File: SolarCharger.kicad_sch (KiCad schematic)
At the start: 45 parts, among them U13 ADM1176-1ARMZ-R7

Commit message: v3.1 Updates
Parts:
- removed R110, R112: 0R, Resistor_SMD:R_0603_1608Metric, symbol Device:R_Small
- C4: renamed from C47; value 3.3nF -> 3n3
- R19: renamed from R25; value 100K -> 100k
- R21: renamed from R35; value 200K -> 200k
- R26: value 100K -> 100k
- R28: renamed from R89; value 200K -> 200k
- R33: renamed from R27; value 100K -> 100k
- R35: renamed from R109; value 200K -> 200k
- R36: renamed from R111; now not fitted
- R37: renamed from R113; now not fitted
- R38: renamed from R124; value ?R -> 0.01R
- R39: renamed from R125; value 1K -> 1k
- renumbered F6 to F2, F7 to F3, F8 to F4, F9 to F5, F10 to F6, R16 to R15, R17 to R16, R13 to R17, R22 to R18, R34 to R20, R18 to R22, R19 to R23, R14 to R24, R23 to R25, R88 to R27, R20 to R29, R21 to R30, R15 to R31, R24 to R32, R108 to R34, U13 to U2
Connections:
- net A0_S renamed A0
- net A1_S renamed A1
- net MPPT1/VIN renamed DSOLAR1
- net MPPT2/VIN renamed DSOLAR2
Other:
- sheet I2C Single Protection4 renamed I2C Single Protection2
- sheet I2C Single Protection5 renamed I2C Single Protection3
- note added: "#TODO: Check Resistor Values"
- note added: "I2C ADDR R36, R37 0R, 0R: 0x40 150k, 0R: 0x41 DNP, DNP: 0x4A 0R, DNP: 0x48"
- note removed: "I2C ADDR 0x4A Install R95: 0x48"
- company: (none) -> Carnegie Mellon University
- title: (none) -> Argus XY Solar Panel
- moved on the sheet: D1, D2, D3, D4, D5, F2, F3, F4, F5, R17, R18, R19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

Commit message: Local Stash
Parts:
- SC1, SC2, SC4, SC5, SC6: value SM141K06TF -> SM141K06TF/S; footprint Argus-Miscellaneous:SM141K06TF -> Argus-Miscellaneous:SM141K06TF_S
- SC3: value SM141K10TF -> SM141K10TF/S; footprint Argus-Miscellaneous:SM141K10TF -> Argus-Miscellaneous:SM141K10TF_S
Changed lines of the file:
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@@
 			)
 		)
-		(property "Value" "SM141K06TF"
+		(property "Value" "SM141K06TF/S"
 			(at 103.378 37.592 90)
 			(effects
@@
 			)
 		)
-		(property "Footprint" "Argus-Miscellaneous:SM141K06TF"
+		(property "Footprint" "Argus-Miscellaneous:SM141K06TF_S"
 			(at 103.124 31.75 90)
 			(effects
@@
 			)
 		)
-		(property "Value" "SM141K06TF"
+		(property "Value" "SM141K06TF/S"
 			(at 88.138 49.022 90)
 			(effects
@@
 			)
 		)
-		(property "Footprint" "Argus-Miscellaneous:SM141K06TF"
+		(property "Footprint" "Argus-Miscellaneous:SM141K06TF_S"
 			(at 87.884 43.18 90)
 			(effects
@@
 			)
 		)
-		(property "Value" "SM141K06TF"
+		(property "Value" "SM141K06TF/S"
 			(at 118.618 37.592 90)
 			(effects
@@
 			)
 		)
-		(property "Footprint" "Argus-Miscellaneous:SM141K06TF"
+		(property "Footprint" "Argus-Miscellaneous:SM141K06TF_S"
 			(at 118.364 31.75 90)
 			(effects
@@
 			)
 		)
-		(property "Value" "SM141K06TF"
+		(property "Value" "SM141K06TF/S"
 			(at 57.658 37.592 90)
 			(effects
@@
 			)
 		)
-		(property "Footprint" "Argus-Miscellaneous:SM141K06TF"
+		(property "Footprint" "Argus-Miscellaneous:SM141K06TF_S"
 			(at 57.404 31.75 90)
 			(effects
@@
 			)
 		)
-		(property "Value" "SM141K06TF"
+		(property "Value" "SM141K06TF/S"
 			(at 72.898 37.592 90)
 			(effects
@@
 			)
 		)
-		(property "Footprint" "Argus-Miscellaneous:SM141K06TF"
+		(property "Footprint" "Argus-Miscellaneous:SM141K06TF_S"
 			(at 72.644 31.75 90)
 			(effects
@@
 			)
 		)
-		(property "Value" "SM141K10TF"
+		(property "Value" "SM141K10TF/S"
 			(at 88.138 37.592 90)
 			(effects
@@
 			)
 		)
-		(property "Footprint" "Argus-Miscellaneous:SM141K10TF"
+		(property "Footprint" "Argus-Miscellaneous:SM141K10TF_S"
 			(at 87.884 31.75 90)
 			(effects

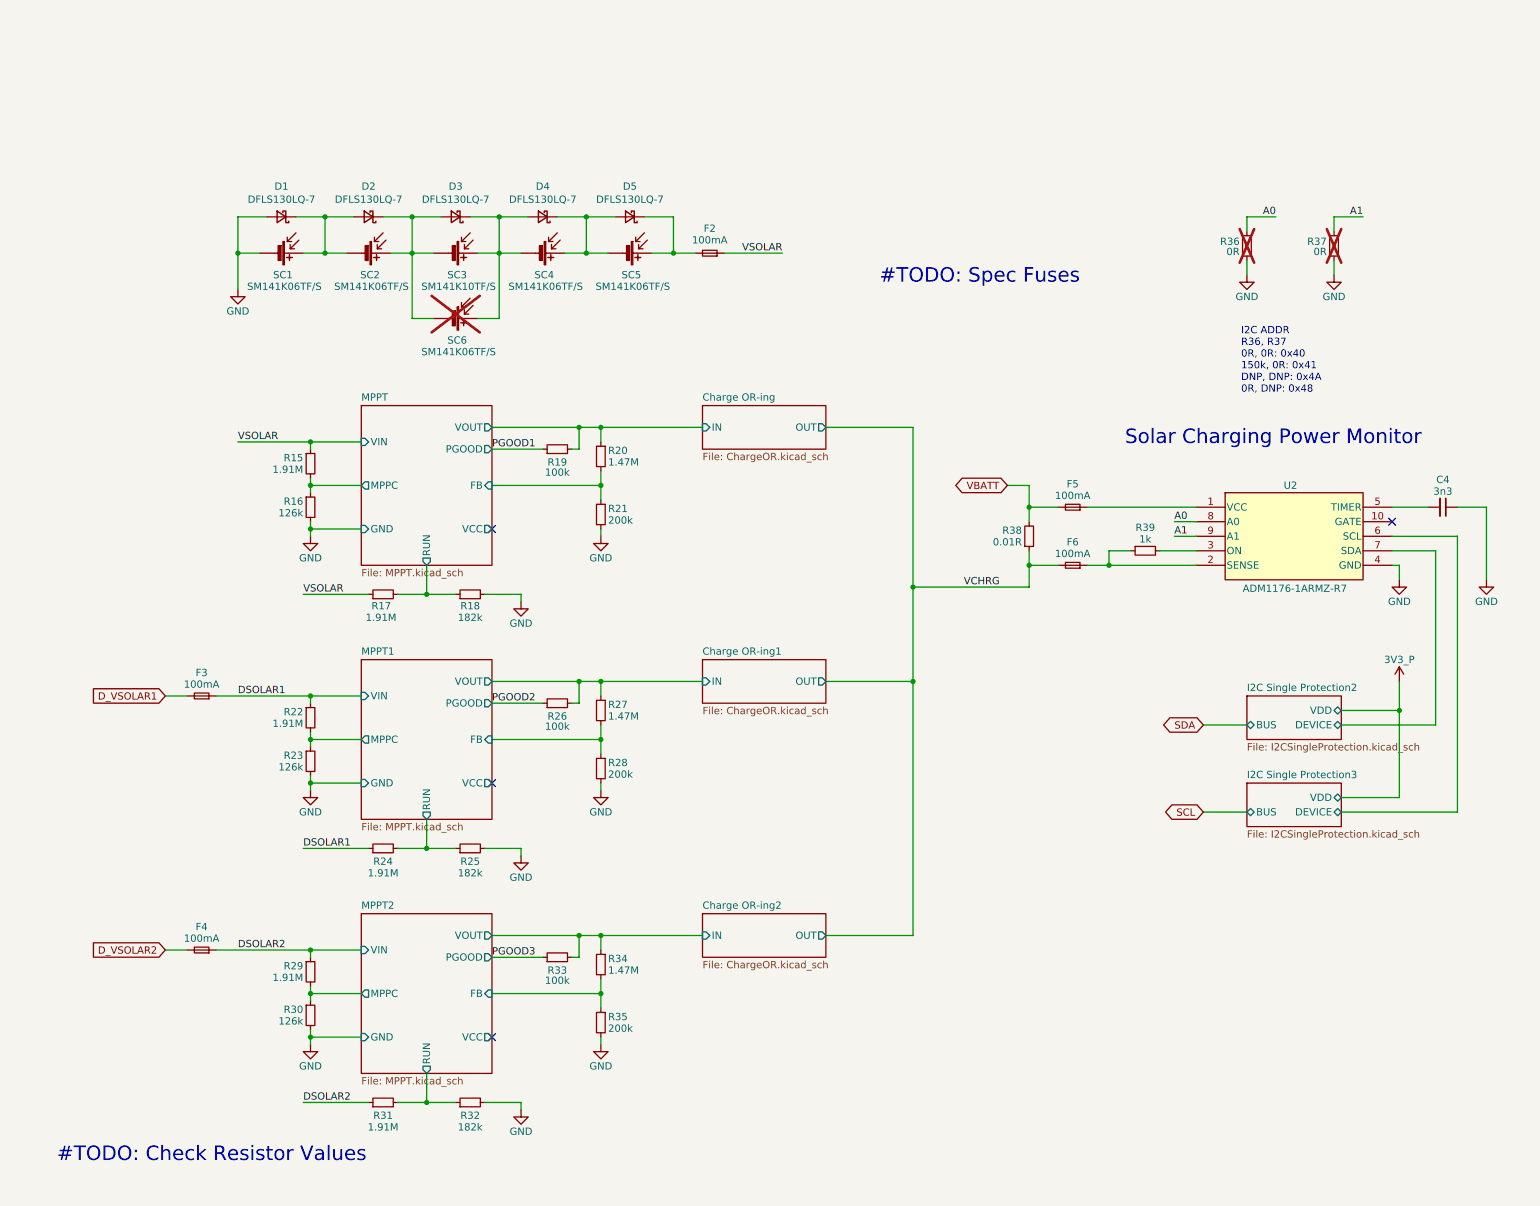
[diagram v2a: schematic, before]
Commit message: Updated access port, added deployment sensor
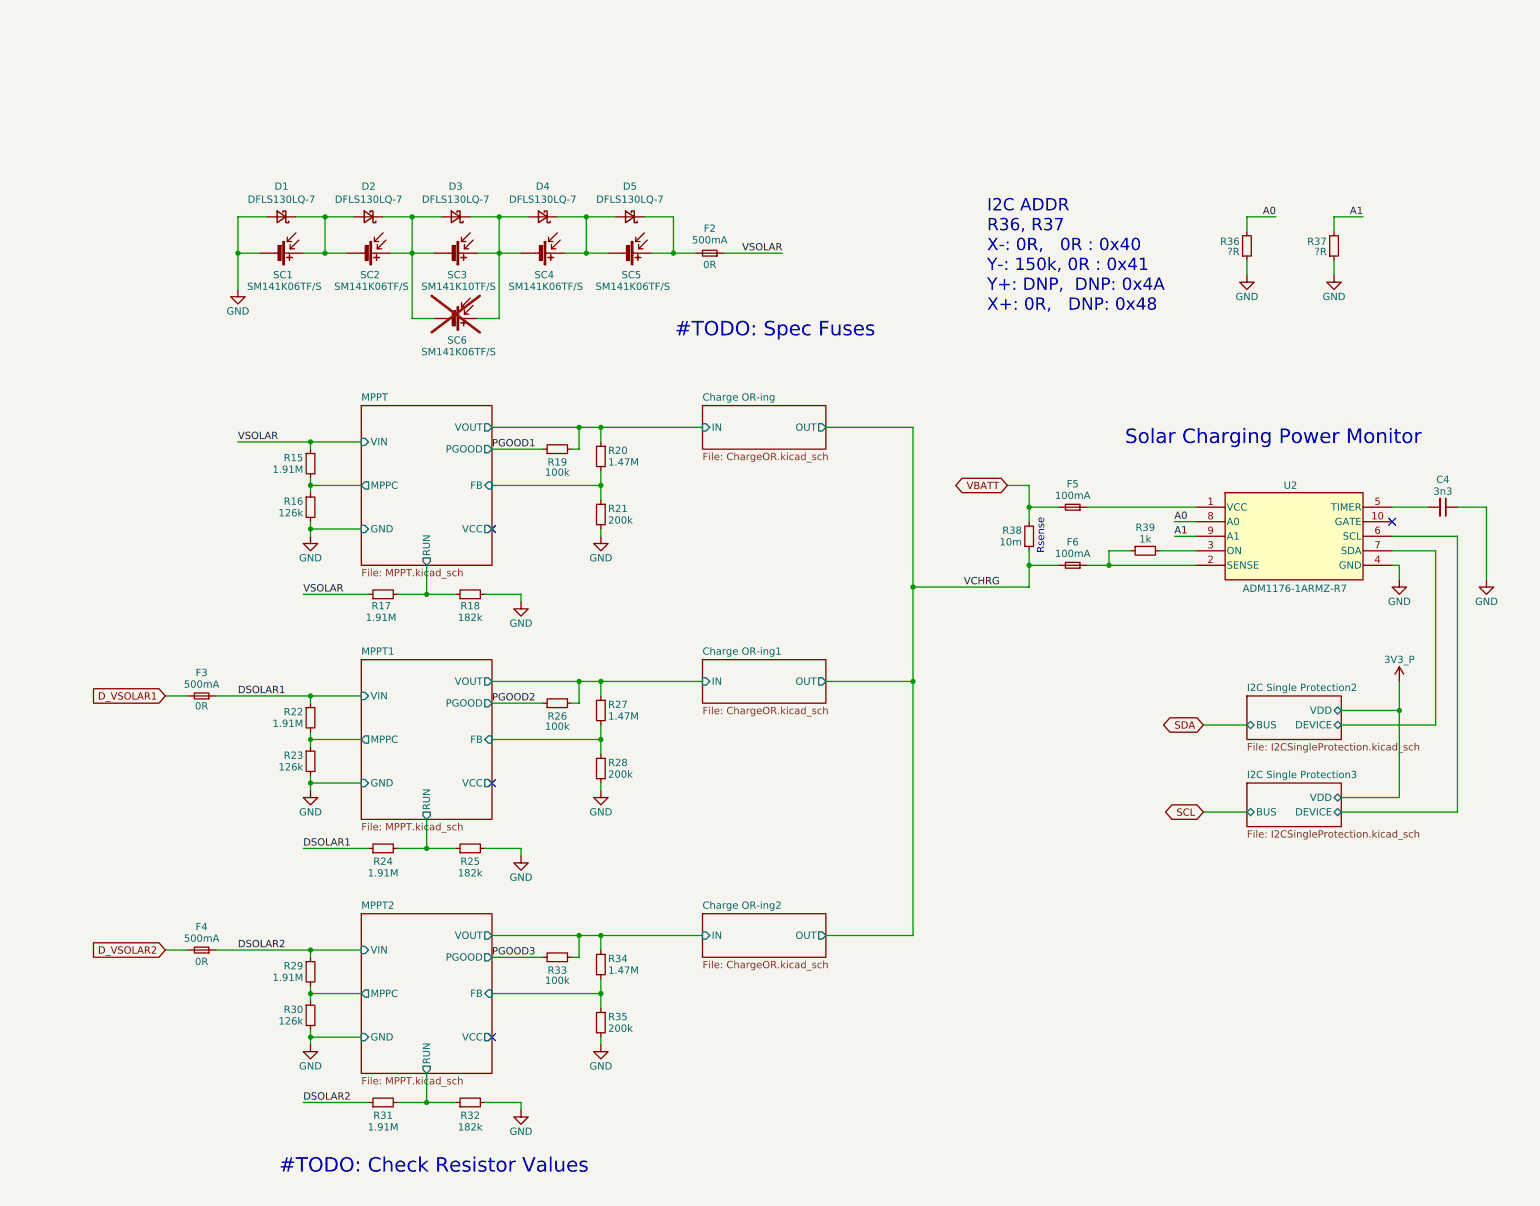
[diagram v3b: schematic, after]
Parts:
- C4: MPN (none) -> C3877267
- F2, F3, F4: value 100mA -> 500mA; Flight (none) -> 0R
- R19, R26, R33: MPN (none) -> C237792
- R21, R28, R35: MPN (none) -> C118142
- R36, R37: value 0R -> ?R; now fitted
- R38: value 0.01R -> 10m; MPN (none) -> C840621
- R39: MPN (none) -> C2484712
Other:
- note added: "I2C ADDR R36, R37 X-: 0R, 0R : 0x40 Y-: 150k, 0R : 0x41 Y+: DNP, DNP: 0x4A X+: 0R, DNP: 0x48"
- note added: "Rsense"
- note removed: "I2C ADDR R36, R37 0R, 0R: 0x40 150k, 0R: 0x41 DNP, DNP: 0x4A 0R, DNP: 0x48"
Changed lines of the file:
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@@
 		(comment 2 "V. Rajesh")
 	)
-	(text "I2C ADDR\nR36, R37\n0R, 0R: 0x40\n150k, 0R: 0x41\nDNP, DNP: 0x4A\n0R, DNP: 0x48\n"
+	(text "I2C ADDR\nR36, R37\nX-: 0R,   0R : 0x40\nY-: 150k, 0R : 0x41\nY+: DNP,  DNP: 0x4A\nX+: 0R,   DNP: 0x48\n"
 		(exclude_from_sim no)
-		(at 225.044 56.388 0)
+		(at 180.594 42.164 0)
 		(effects
 			(font
-				(size 1.27 1.27)
+				(size 2.159 2.159)
 			)
 			(justify left bottom)
 		)
 	)
+	(text "Rsense"
+		(exclude_from_sim no)
+		(at 189.992 81.28 90)
+		(effects
+			(font
+				(size 1.27 1.27)
+			)
+		)
+	)
 	(text "#TODO: Check Resistor Values"
 		(exclude_from_sim no)
-		(at 44.958 189.484 0)
+		(at 83.82 191.516 0)
 		(effects
 			(font
@@
 	(text "#TODO: Spec Fuses"
 		(exclude_from_sim no)
-		(at 179.324 35.814 0)
+		(at 143.51 45.212 0)
 		(effects
 			(font
@@
 			)
 		)
+		(property "MPN" "C237792"
+			(at 105.41 66.04 90)
+			(effects
+				(font
+					(size 1.27 1.27)
+				)
+				(hide yes)
+			)
+		)
 		(pin "1"
 		)
@@
 			)
 		)
+		(property "MPN" "C3877267"
+			(at 260.35 76.2 90)
+			(effects
+				(font
+					(size 1.27 1.27)
+				)
+				(hide yes)
+			)
+		)
 		(pin "1"
 		)
@@
 			)
 		)
+		(property "MPN" "C2484712"
+			(at 208.28 83.82 90)
+			(effects
+				(font
+					(size 1.27 1.27)
+				)
+				(hide yes)
+			)
+		)
 		(pin "1"
 		)
@@
 			)
 		)
-		(property "Value" "100mA"
+		(property "Value" "500mA"
 			(at 43.18 151.638 0)
 			(effects
@@
 			)
 		)
+		(property "Flight" "0R"
+			(at 43.18 155.702 0)
+			(effects
+				(font
+					(size 1.27 1.27)
+				)
+			)
+		)
 		(pin "2"
 		)
@@
 			)
 		)
-		(property "Value" "100mA"
+		(property "Value" "500mA"
 			(at 43.18 107.188 0)
 			(effects
@@
 			)
 		)
+		(property "Flight" "0R"
+			(at 43.18 110.998 0)
+			(effects
+				(font
+					(size 1.27 1.27)
+				)
+			)
+		)
 		(pin "2"
 		)
@@
 		(in_bom yes)
 		(on_board yes)
-		(dnp yes)
+		(dnp no)
 		(property "Reference" "R37"
 			(at 240.03 29.718 0)
@@
 			)
 		)
-		(property "Value" "0R"
+		(property "Value" "?R"
 			(at 240.03 31.496 0)
 			(effects
@@
 			)
 		)
+		(property "MPN" "C237792"
+			(at 105.41 110.49 90)
+			(effects
+				(font
+					(size 1.27 1.27)
+				)
+				(hide yes)
+			)
+		)
 		(pin "1"
 		)
@@
 			)
 		)
+		(property "MPN" "C118142"
+			(at 113.03 166.37 0)
+			(effects
+				(font
+					(size 1.27 1.27)
+				)
+				(hide yes)
+			)
+		)
 		(pin "1"
 		)
@@
 		(in_bom yes)
 		(on_board yes)
-		(dnp yes)
+		(dnp no)
 		(property "Reference" "R36"
 			(at 224.79 29.718 0)
@@
 			)
 		)
-		(property "Value" "0R"
+		(property "Value" "?R"
 			(at 224.79 31.496 0)
 			(effects
@@
 			)
 		)
-		(property "Value" "100mA"
+		(property "Value" "500mA"
 			(at 132.08 29.464 0)
 			(effects
@@
 			)
 		)
+		(property "Flight" "0R"
+			(at 132.08 33.782 0)
+			(effects
+				(font
+					(size 1.27 1.27)
+				)
+			)
+		)
 		(pin "2"
 		)
@@
 			)
 		)
+		(property "MPN" "C118142"
+			(at 113.03 77.47 0)
+			(effects
+				(font
+					(size 1.27 1.27)
+				)
+				(hide yes)
+			)
+		)
 		(pin "1"
 		)
@@
 			)
 		)
-		(property "Value" "0.01R"
+		(property "Value" "10m"
 			(at 186.69 82.296 0)
 			(effects
@@
 			)
 		)
+		(property "MPN" "C840621"
+			(at 187.96 81.28 0)
+			(effects
+				(font
+					(size 1.27 1.27)
+				)
+				(hide yes)
+			)
+		)
 		(pin "1"
 		)
@@
 			)
 		)
+		(property "MPN" "C237792"
+			(at 105.41 154.94 90)
+			(effects
+				(font
+					(size 1.27 1.27)
+				)
+				(hide yes)
+			)
+		)
 		(pin "1"
 		)
@@
 			(at 113.03 121.92 0)
 			(effects
+				(font
+					(size 1.27 1.27)
+				)
+				(hide yes)
+			)
+		)
+		(property "MPN" "C118142"
+			(at 113.03 121.92 0)
+			(effects

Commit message: Local Stash
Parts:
- added R118, R119, R120: 0R, Resistor_SMD:R_0603_1608Metric, symbol Device:R_Small
- R15: value 1.91M -> 1.8M; now not fitted; now left out of the parts list
- R16: value 126k -> 100k; now not fitted; now left out of the parts list
- R17: value 1.91M -> 2.10M
- R18: value 182k -> 137k
- R20, R27, R34: value 1.47M -> 2M
- R21, R28, R35: value 200k -> 270k
- R22, R29: value 1.91M -> 2M; now not fitted; now left out of the parts list
- R23, R30: value 126k -> 127k; now not fitted; now left out of the parts list
- R24, R31: value 1.91M -> 1.87M
- R25, R32: value 182k -> 140k
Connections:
- net MPPT/VCC: now also R120.1
- net MPPT1/VCC: now also R118.1
- net MPPT2/VCC: now also R119.1
- net MPPT/MPPC renamed MPPC
- net MPPC: now also R120.2
- net MPPT1/MPPC renamed MPPC1
- net MPPC1: now also R118.2
- net MPPT2/MPPC renamed MPPC2
- net MPPC2: now also R119.2
- no-connect marks 4 -> 1
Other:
- note added: "DNP if using MPPC"
- note added: "Use if populating SC3 V_in(mppc) = 1.00 * (1 + R15 / R16) V_in(mppc) = 1.00 * (1 + 1.8M / 100k) V_in(mppc) = 1.00 * (1 + 18) V_in(mppc) = 19.0V"
- note added: "Use if populating SC6 V_in(mppc) = 1.00 * (1 + R15 / R16) V_in(mppc) = 1.00 * (1 + 2M / 127k) V_in(mppc) = 1.00 * (1 + 15.75) V_in(mppc) = 16.75V"
- note added: "V_in(mppc) = 1.00 * (1 + R22 / R23) V_in(mppc) = 1.00 * (1 + 2M / 127k) V_in(mppc) = 1.00 * (1 + 15.75) V_in(mppc) = 16.75V"
- note added: "V_in(mppc) = 1.00 * (1 + R29 / R30) V_in(mppc) = 1.00 * (1 + 2M / 127k) V_in(mppc) = 1.00 * (1 + 15.75) V_in(mppc) = 16.75V"
- note added: "V_in(turnon) = 1.05 * (1 + R17 / R18) V_in(turnon) = 1.05 * (1 + 1.87M / 140k) V_in(turnon) = 1.05 * (1 + 13.36) V_in(turnon) = 15.08V"
- note added: "V_in(turnon) = 1.05 * (1 + R17 / R18) V_in(turnon) = 1.05 * (1 + 2.10M / 137k) V_in(turnon) = 1.05 * (1 + 15.33) V_in(turnon) = 17.15V"
- note added: "V_in(turnon) = 1.05 * (1 + R24 / R25) V_in(turnon) = 1.05 * (1 + 1.87M / 140k) V_in(turnon) = 1.05 * (1 + 13.36) V_in(turnon) = 15.08V"
- note added: "V_in(turnon) = 1.05 * (1 + R31 / R32) V_in(turnon) = 1.05 * (1 + 1.87M / 140k) V_in(turnon) = 1.05 * (1 + 13.36) V_in(turnon) = 15.08V"
- note added: "V_out = 1.00 * (1 + R20 / R21) V_out = 1.00 * (1 + 2M / 270k) V_out = 1.00 * (1 + 7.41) V_out = 8.41V"
- note added: "V_out = 1.00 * (1 + R27 / R28) V_out = 1.00 * (1 + 2M / 270k) V_out = 1.00 * (1 + 7.41) V_out = 8.41V"
- note added: "V_out = 1.00 * (1 + R34 / R35) V_out = 1.00 * (1 + 2M / 270k) V_out = 1.00 * (1 + 7.41) V_out = 8.41V"
